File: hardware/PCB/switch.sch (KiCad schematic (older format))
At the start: 150 parts

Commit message: outline done
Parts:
- CherryMX1, CherryMX10, CherryMX11, CherryMX12, CherryMX13, CherryMX14, CherryMX15, CherryMX16, CherryMX17, CherryMX18, CherryMX19, CherryMX2, CherryMX20, CherryMX21, CherryMX22, CherryMX23, CherryMX24, CherryMX25, CherryMX26, CherryMX27, CherryMX28, CherryMX29, CherryMX3, CherryMX30, CherryMX31, CherryMX32, CherryMX33, CherryMX34, CherryMX35, CherryMX36, CherryMX37, CherryMX38, CherryMX39, CherryMX4, CherryMX40, CherryMX41, CherryMX42, CherryMX43, CherryMX44, CherryMX45, CherryMX46, CherryMX47, CherryMX48, CherryMX49, CherryMX5, CherryMX50, CherryMX51, CherryMX52, CherryMX53, CherryMX54, CherryMX55, CherryMX56, CherryMX57, CherryMX58, CherryMX59, CherryMX6, CherryMX60, CherryMX61, CherryMX62, CherryMX63, CherryMX64, CherryMX65, CherryMX66, CherryMX67, CherryMX68, CherryMX7, CherryMX8, CherryMX9: footprint keyswitches:Kailh_socket_MX_optional_reversible -> keyswitches:Kailh_socket_MX

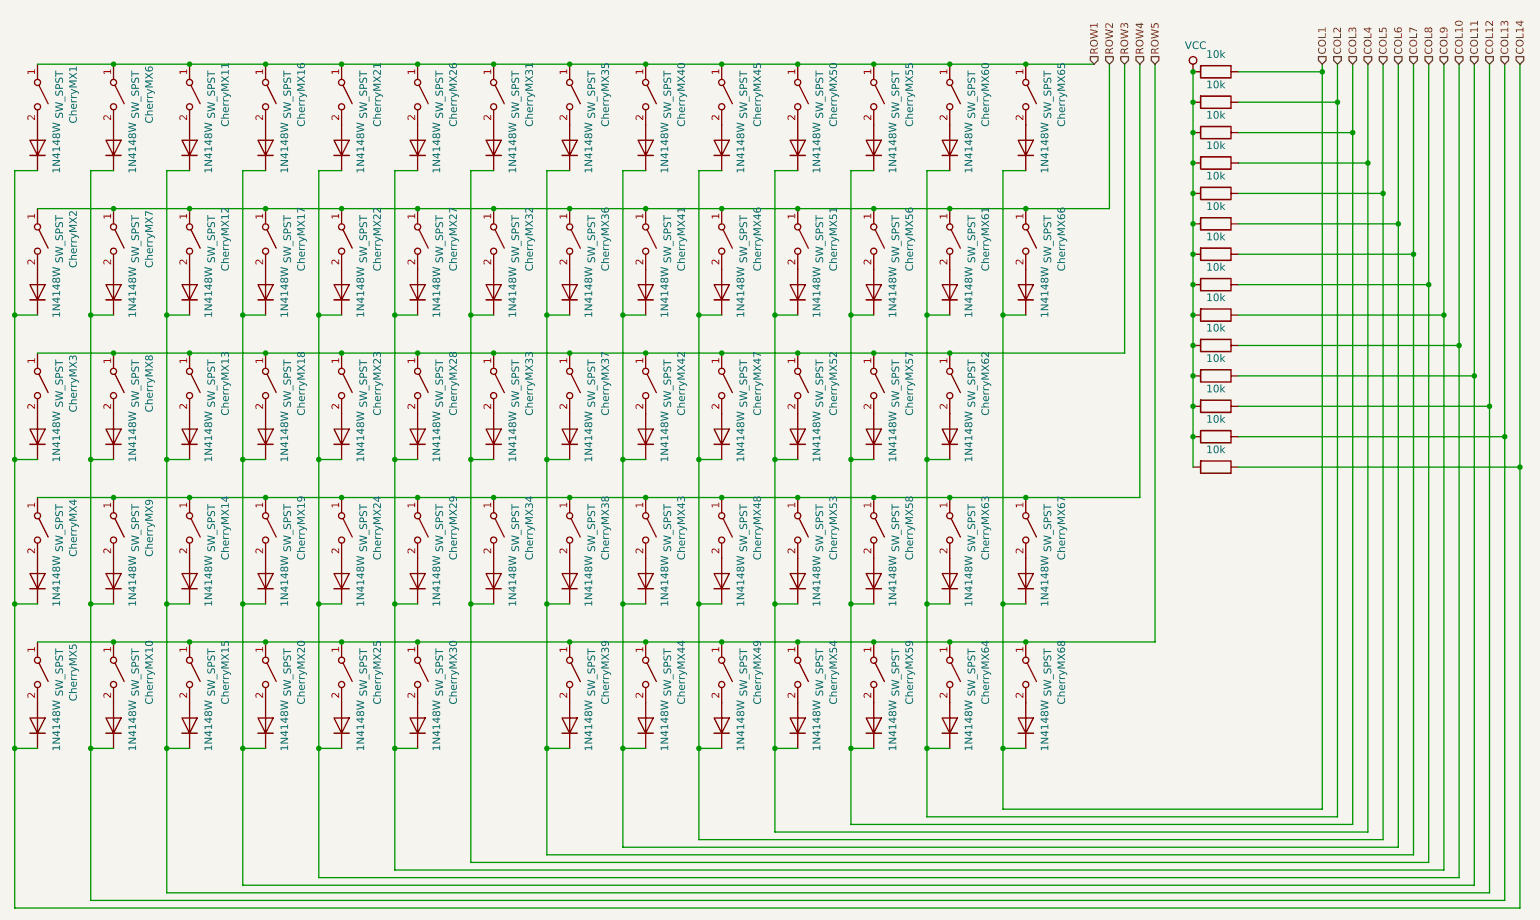
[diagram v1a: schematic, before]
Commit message: Line up most parts and fix some problems with the part
1.Fix the LED footprint size
2.Edit the hotplug to be simpler (removed 2 holes)
3.Line up everything and the silkscreen
4. Fix the LED matrix and the switch matrix sch
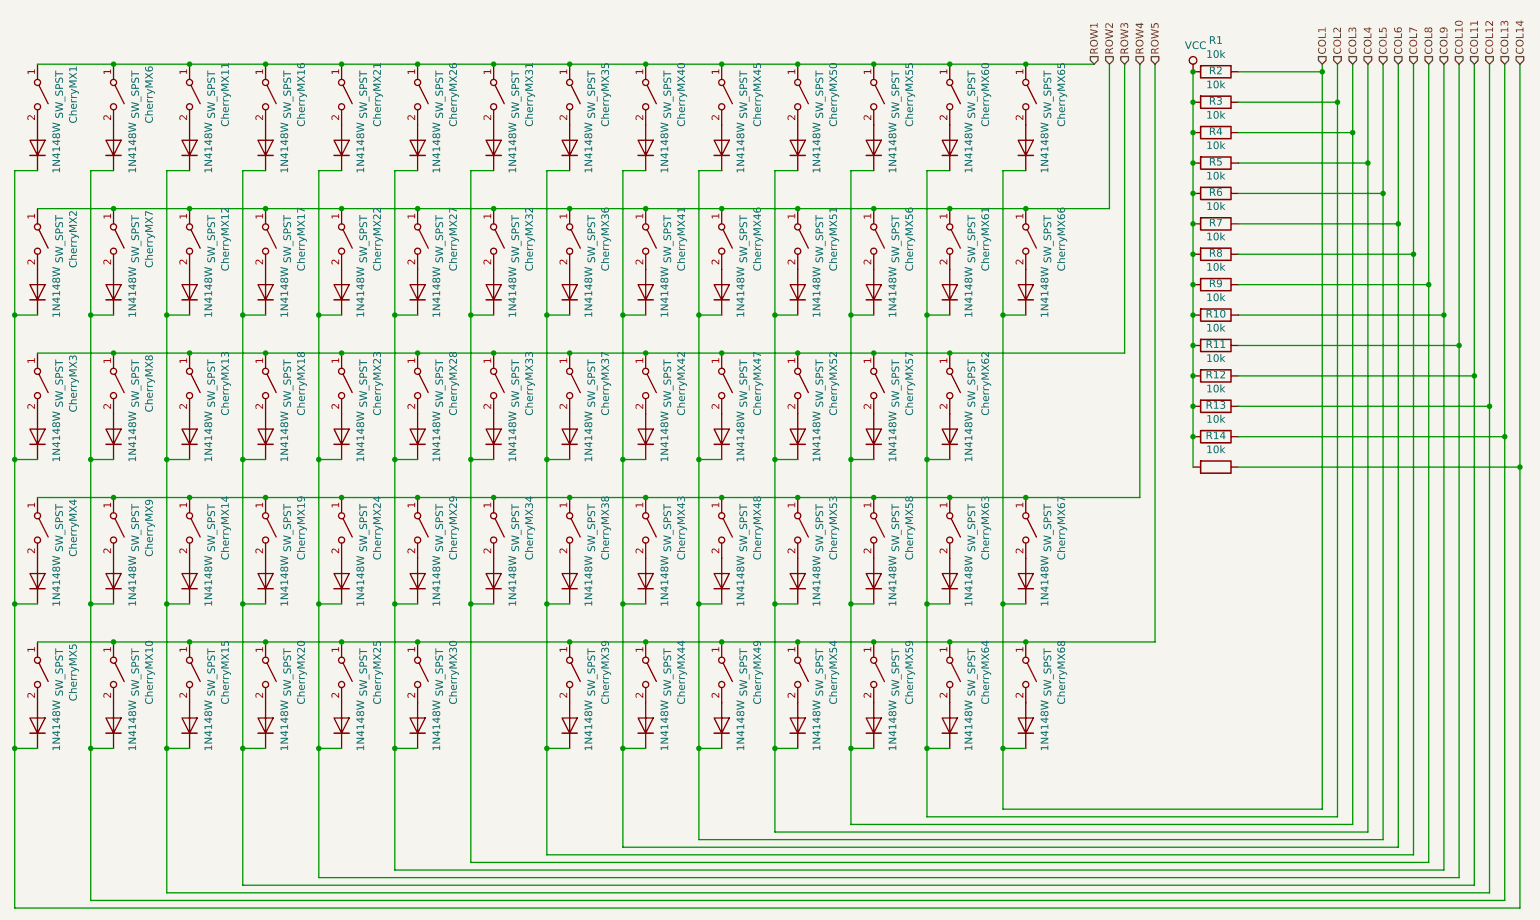
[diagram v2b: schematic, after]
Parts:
- CherryMX1, CherryMX10, CherryMX11, CherryMX12, CherryMX13, CherryMX14, CherryMX15, CherryMX16, CherryMX17, CherryMX18, CherryMX19, CherryMX2, CherryMX20, CherryMX21, CherryMX22, CherryMX23, CherryMX24, CherryMX25, CherryMX26, CherryMX27, CherryMX28, CherryMX29, CherryMX3, CherryMX30, CherryMX31, CherryMX32, CherryMX33, CherryMX34, CherryMX35, CherryMX36, CherryMX37, CherryMX38, CherryMX39, CherryMX4, CherryMX40, CherryMX41, CherryMX42, CherryMX43, CherryMX44, CherryMX45, CherryMX46, CherryMX47, CherryMX48, CherryMX49, CherryMX5, CherryMX50, CherryMX51, CherryMX52, CherryMX53, CherryMX54, CherryMX55, CherryMX56, CherryMX57, CherryMX58, CherryMX59, CherryMX6, CherryMX60, CherryMX61, CherryMX62, CherryMX63, CherryMX64, CherryMX65, CherryMX66, CherryMX67, CherryMX68, CherryMX7, CherryMX8, CherryMX9: footprint keyswitches:Kailh_socket_MX -> KiCad:Kailh_socket_MX_simplified

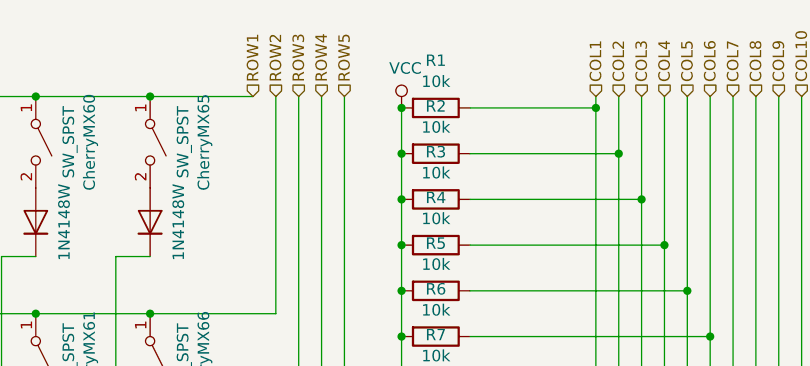
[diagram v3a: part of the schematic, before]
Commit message: Make it better by get rid of the protonC
1. Remove protonC. use STM32F303CCT6 instead
2.Use parts based on avalibility
3.Extend the case so it now fits more parts( should be big enough
4. A reasonable USB connector
5. Probably a working DC-DC solution to providde 3.3V
6. Move 3733's 5V to only 3.3V (maybe it won't work?)
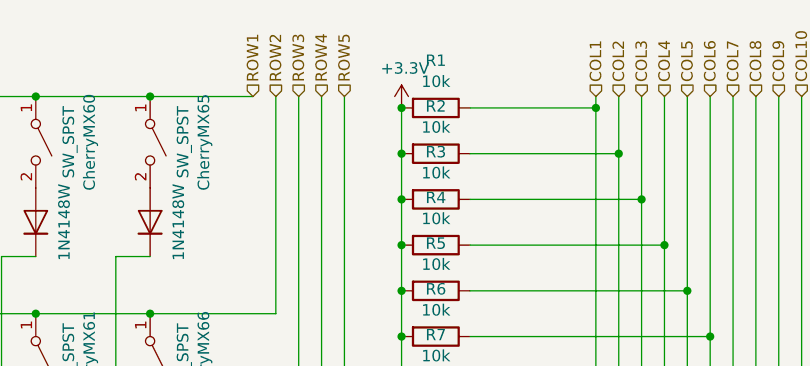
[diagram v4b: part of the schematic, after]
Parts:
- D1, D10, D11, D12, D13, D14, D15, D16, D17, D18, D19, D2, D20, D21, D22, D23, D24, D25, D26, D27, D28, D29, D3, D30, D31, D32, D33, D34, D35, D36, D37, D38, D39, D4, D40, D41, D42, D43, D44, D45, D46, D47, D48, D49, D5, D50, D51, D52, D53, D54, D55, D56, D57, D58, D59, D6, D60, D61, D62, D63, D64, D65, D66, D67, D68, D7, D8, D9: footprint Diode_SMD:D_SOD-123 -> Diode_SMD:D_SOD-323
- R1, R10, R11, R12, R13, R14, R2, R3, R4, R5, R6, R7, R8, R9: footprint Resistor_SMD:R_0603_1608Metric_Pad1.05x0.95mm_HandSolder -> Resistor_SMD:R_0603_1608Metric
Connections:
- net VCC renamed +3V3

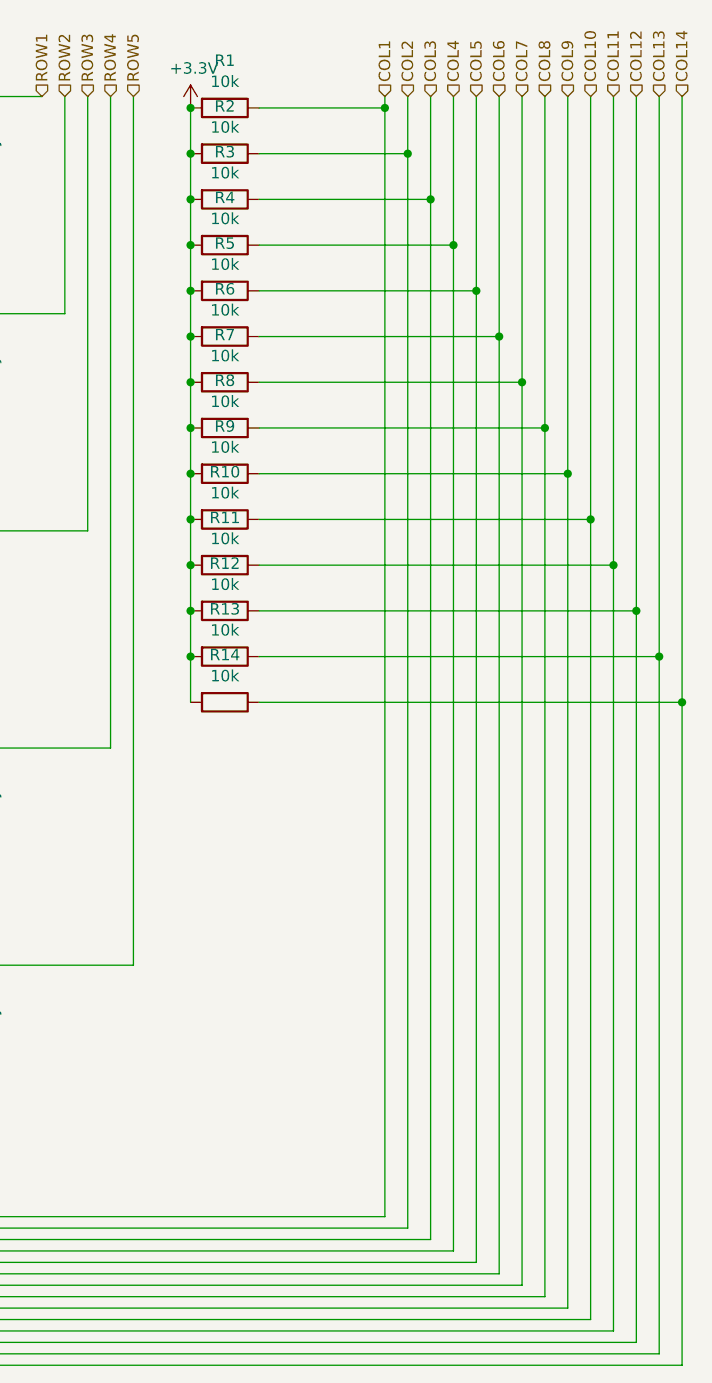
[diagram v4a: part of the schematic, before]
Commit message: I think I don't need those pull ups, if i really need it, add them later
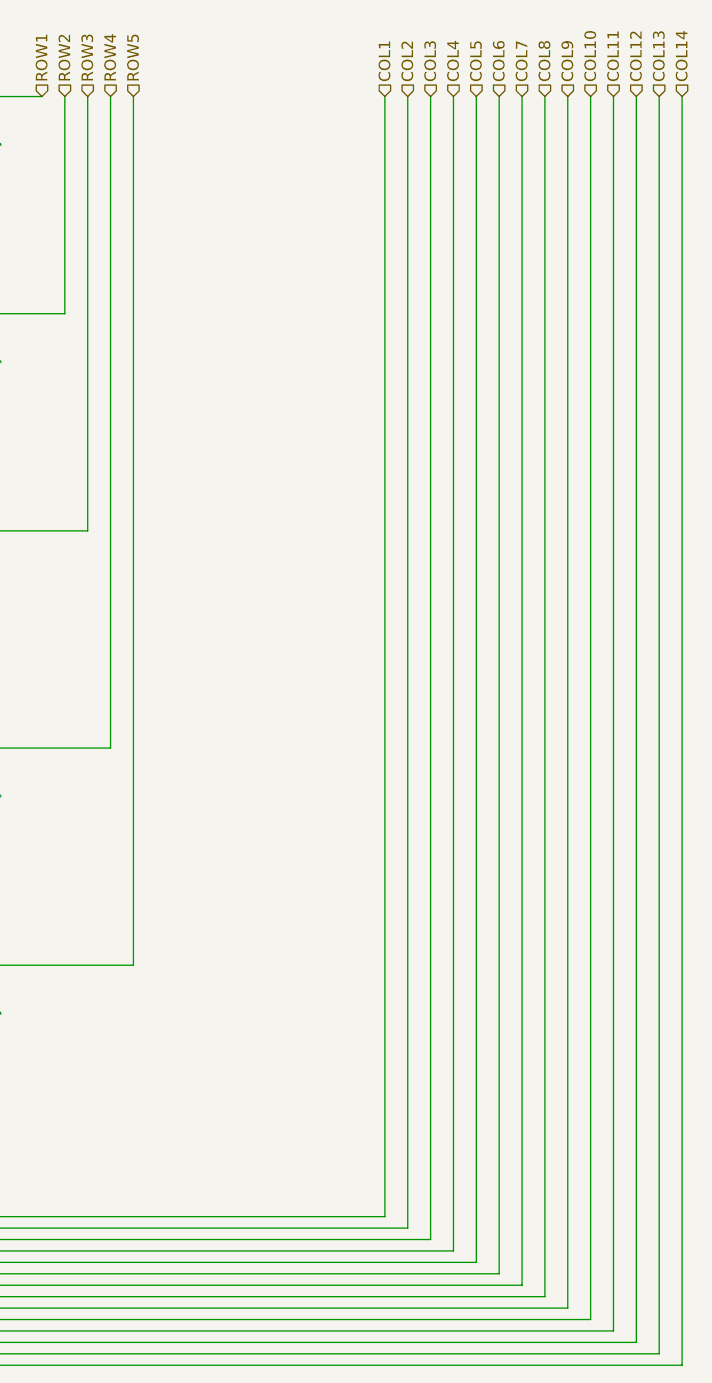
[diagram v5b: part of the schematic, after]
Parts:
- removed R1, R10, R11, R12, R13, R14, R2, R3, R4, R5, R6, R7, R8, R9: 10k, Resistor_SMD:R_0603_1608Metric, symbol Device:R

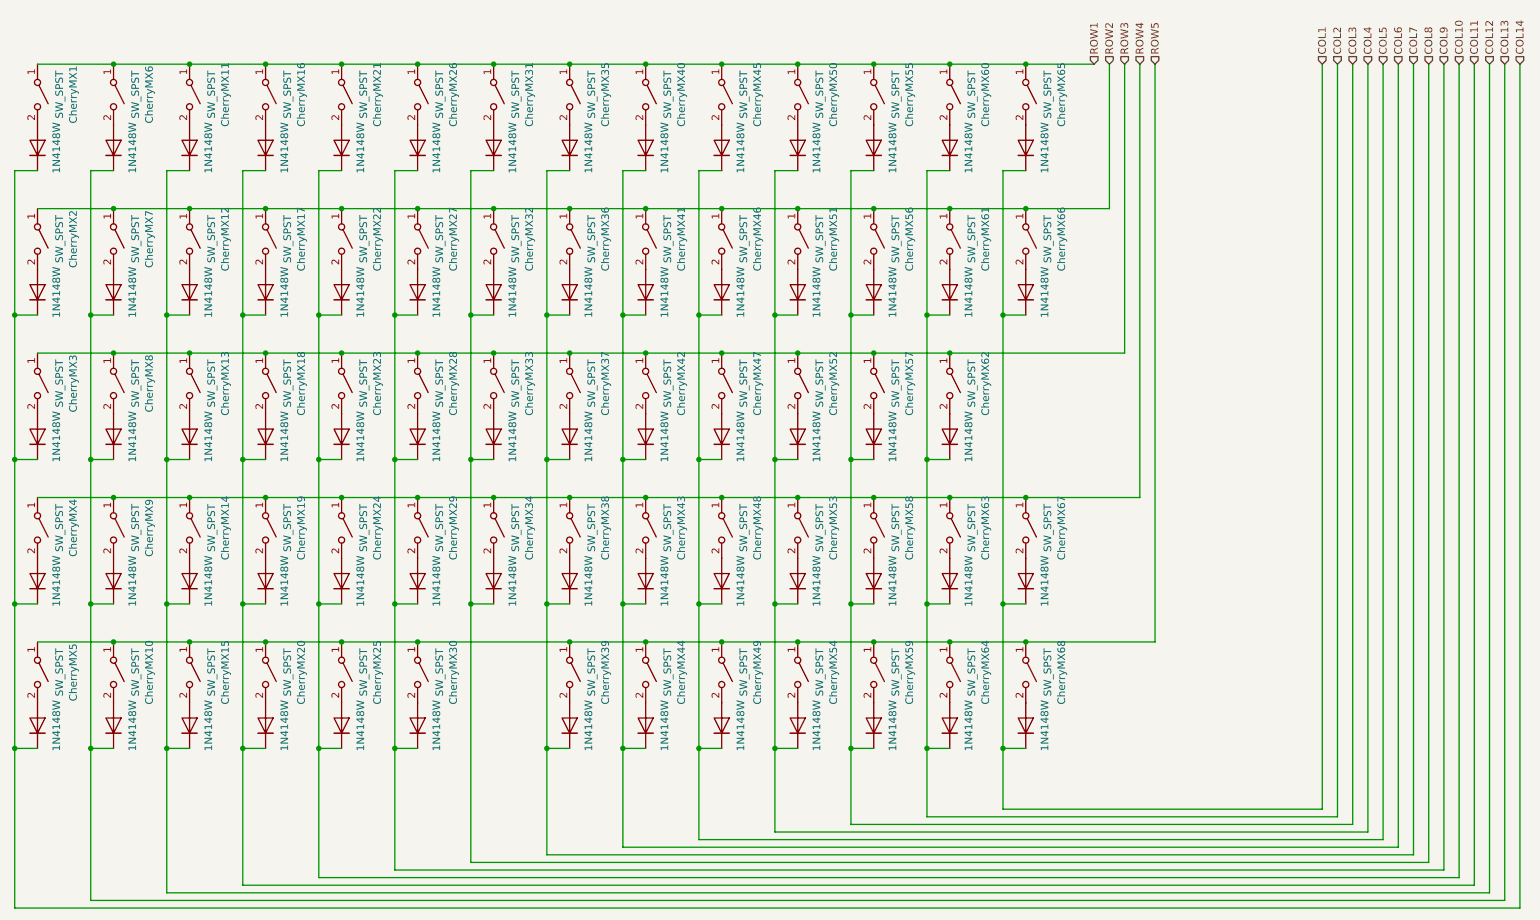
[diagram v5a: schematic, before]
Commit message: Rotate the RGB controller. gonna have a lot of work to do
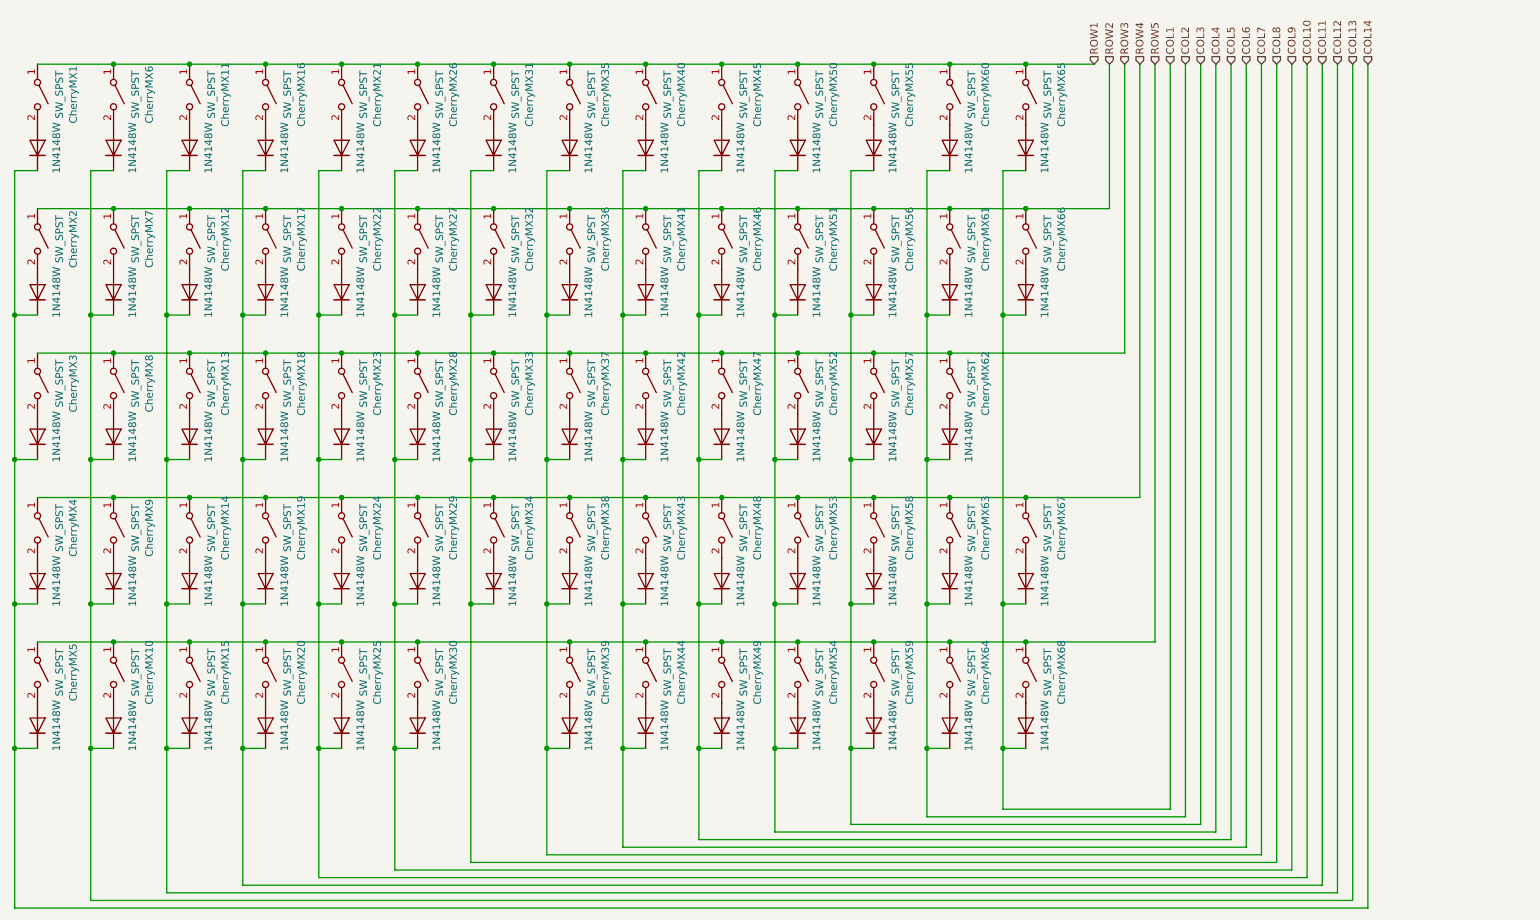
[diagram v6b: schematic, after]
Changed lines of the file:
@@
 Connection ~ 3850 4750
 Connection ~ 4850 4750
+Text HLabel 8800 950  1    50   Input ~ 0
+COL1
+Text HLabel 8900 950  1    50   Input ~ 0
+COL2
+Text HLabel 9000 950  1    50   Input ~ 0
+COL3
+Text HLabel 9100 950  1    50   Input ~ 0
+COL4
+Text HLabel 9200 950  1    50   Input ~ 0
+COL5
+Text HLabel 9300 950  1    50   Input ~ 0
+COL6
+Text HLabel 9400 950  1    50   Input ~ 0
+COL7
+Text HLabel 9500 950  1    50   Input ~ 0
+COL8
+Text HLabel 9600 950  1    50   Input ~ 0
+COL9
+Text HLabel 9700 950  1    50   Input ~ 0
+COL10
 Text HLabel 9800 950  1    50   Input ~ 0
-COL1
+COL11
 Text HLabel 9900 950  1    50   Input ~ 0
-COL2
+COL12
 Text HLabel 10000 950  1    50   Input ~ 0
-COL3
+COL13
 Text HLabel 10100 950  1    50   Input ~ 0
-COL4
-Text HLabel 10200 950  1    50   Input ~ 0
-COL5
-Text HLabel 10300 950  1    50   Input ~ 0
-COL6
-Text HLabel 10400 950  1    50   Input ~ 0
-COL7
-Text HLabel 10500 950  1    50   Input ~ 0
-COL8
-Text HLabel 10600 950  1    50   Input ~ 0
-COL9
-Text HLabel 10700 950  1    50   Input ~ 0
-COL10
-Text HLabel 10800 950  1    50   Input ~ 0
-COL11
-Text HLabel 10900 950  1    50   Input ~ 0
-COL12
-Text HLabel 11000 950  1    50   Input ~ 0
-COL13
-Text HLabel 11100 950  1    50   Input ~ 0
 COL14
 Wire Wire Line
@@
 Connection ~ 7700 5450
 Wire Wire Line
-	7700 5850 9800 5850
+	7700 5850 8800 5850
 Wire Wire Line
-	7200 5900 9900 5900
+	7200 5900 8900 5900
 Wire Wire Line
-	6700 5950 10000 5950
+	6700 5950 9000 5950
 Wire Wire Line
-	6200 6000 10100 6000
+	6200 6000 9100 6000
 Wire Wire Line
-	5700 6050 10200 6050
+	5700 6050 9200 6050
 Wire Wire Line
-	5200 6100 10300 6100
+	5200 6100 9300 6100
 Wire Wire Line
-	4700 6150 10400 6150
+	4700 6150 9400 6150
 Wire Wire Line
-	4200 6200 10500 6200
+	4200 6200 9500 6200
 Wire Wire Line
-	3700 6250 10600 6250
+	3700 6250 9600 6250
 Wire Wire Line
-	3200 6300 10700 6300
+	3200 6300 9700 6300
 Wire Wire Line
-	2700 6350 10800 6350
+	2700 6350 9800 6350
 Connection ~ 7850 950
 Wire Wire Line
@@
 	8700 950  8700 4750
 Wire Wire Line
-	10900 6400 2200 6400
+	1700 6450 10000 6450
 Wire Wire Line
-	1700 6450 11000 6450
+	9700 950  9700 6300
 Wire Wire Line
-	11100 6500 1200 6500
+	9600 950  9600 6250
 Wire Wire Line
-	11100 950  11100 6500
+	9500 950  9500 6200
 Wire Wire Line
-	11000 950  11000 6450
+	9400 950  9400 6150
 Wire Wire Line
-	10900 950  10900 6400
+	9300 950  9300 6100
 Wire Wire Line
-	10800 950  10800 6350
+	9200 950  9200 6050
 Wire Wire Line
-	10700 950  10700 6300
+	9100 950  9100 6000
 Wire Wire Line
-	10600 950  10600 6250
+	9000 950  9000 5950
 Wire Wire Line
-	10500 950  10500 6200
+	8900 950  8900 5900
 Wire Wire Line
-	10400 950  10400 6150
+	8800 950  8800 5850
 Wire Wire Line
-	10300 950  10300 6100
+	9900 6400 2200 6400
 Wire Wire Line
-	10200 950  10200 6050
+	10100 6500 1200 6500
 Wire Wire Line
-	10100 950  10100 6000
+	9800 950  9800 6350
 Wire Wire Line
-	10000 950  10000 5950
+	9900 950  9900 6400
 Wire Wire Line
-	9900 950  9900 5900
+	10000 950  10000 6450
 Wire Wire Line
-	9800 950  9800 5850
+	10100 950  10100 6500
 $EndSCHEMATC

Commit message: alot of changes
modify the QFN-48 so PCB 3d view in future would look better (so I don't design a part that doesn't fit)
I made a useless QFN-40 3d model
modify schematics so it looks better
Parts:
- D1, D10, D11, D12, D13, D14, D15, D16, D17, D18, D19, D2, D20, D21, D22, D23, D24, D25, D26, D27, D28, D29, D3, D30, D31, D32, D33, D34, D35, D36, D37, D38, D39, D4, D40, D41, D42, D43, D44, D45, D46, D47, D48, D49, D5, D50, D51, D52, D53, D54, D55, D56, D57, D58, D59, D6, D60, D61, D62, D63, D64, D65, D66, D67, D68, D7, D8, D9: Footprint Diode_SMD:D_SOD-123 -> Diode_SMD:D_SOD-323; Value (none) -> 1N4148W

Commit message: I guess it is done, maybe just make it?
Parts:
- renumbered CherryMX1 to Key1, CherryMX10 to Key10, CherryMX11 to Key11, CherryMX12 to Key12, CherryMX13 to Key13, CherryMX14 to Key14, CherryMX15 to Key15, CherryMX16 to Key16, CherryMX17 to Key17, CherryMX18 to Key18, CherryMX19 to Key19, CherryMX2 to Key2, CherryMX20 to Key20, CherryMX21 to Key21, CherryMX22 to Key22, CherryMX23 to Key23, CherryMX24 to Key24, CherryMX25 to Key25, CherryMX26 to Key26, CherryMX27 to Key27, CherryMX28 to Key28, CherryMX29 to Key29, CherryMX3 to Key3, CherryMX30 to Key30, CherryMX31 to Key31, CherryMX32 to Key32, CherryMX33 to Key33, CherryMX34 to Key34, CherryMX35 to Key35, CherryMX36 to Key36, CherryMX37 to Key37, CherryMX38 to Key38, CherryMX39 to Key39, CherryMX4 to Key4, CherryMX40 to Key40, CherryMX41 to Key41, CherryMX42 to Key42, CherryMX43 to Key43, CherryMX44 to Key44, CherryMX45 to Key45, CherryMX46 to Key46, CherryMX47 to Key47, CherryMX48 to Key48, CherryMX49 to Key49, CherryMX5 to Key5, CherryMX50 to Key50, CherryMX51 to Key51, CherryMX52 to Key52, CherryMX53 to Key53, CherryMX54 to Key54, CherryMX55 to Key55, CherryMX56 to Key56, CherryMX57 to Key57, CherryMX58 to Key58, CherryMX59 to Key59, CherryMX6 to Key6, CherryMX60 to Key60, CherryMX61 to Key61, CherryMX62 to Key62, CherryMX63 to Key63, CherryMX64 to Key64, CherryMX65 to Key65, CherryMX66 to Key66, CherryMX67 to Key67, CherryMX68 to Key68, CherryMX7 to Key7, CherryMX8 to Key8, CherryMX9 to Key9
